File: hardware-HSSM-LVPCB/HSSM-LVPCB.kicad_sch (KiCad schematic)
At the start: 56 parts, among them J1 UFL_R_SMT_1_10, J2 LPPB061NGCN-RC, Q1 Q_MOSFET_N_BSS123, Q2 Q_MOSFET_N_BSS123, U1 ESP32-C6, U2 W25Q64JVSSIQ_SOIC-8, X1 X_40MHz_SMD_ECS-2520SMV-400-F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

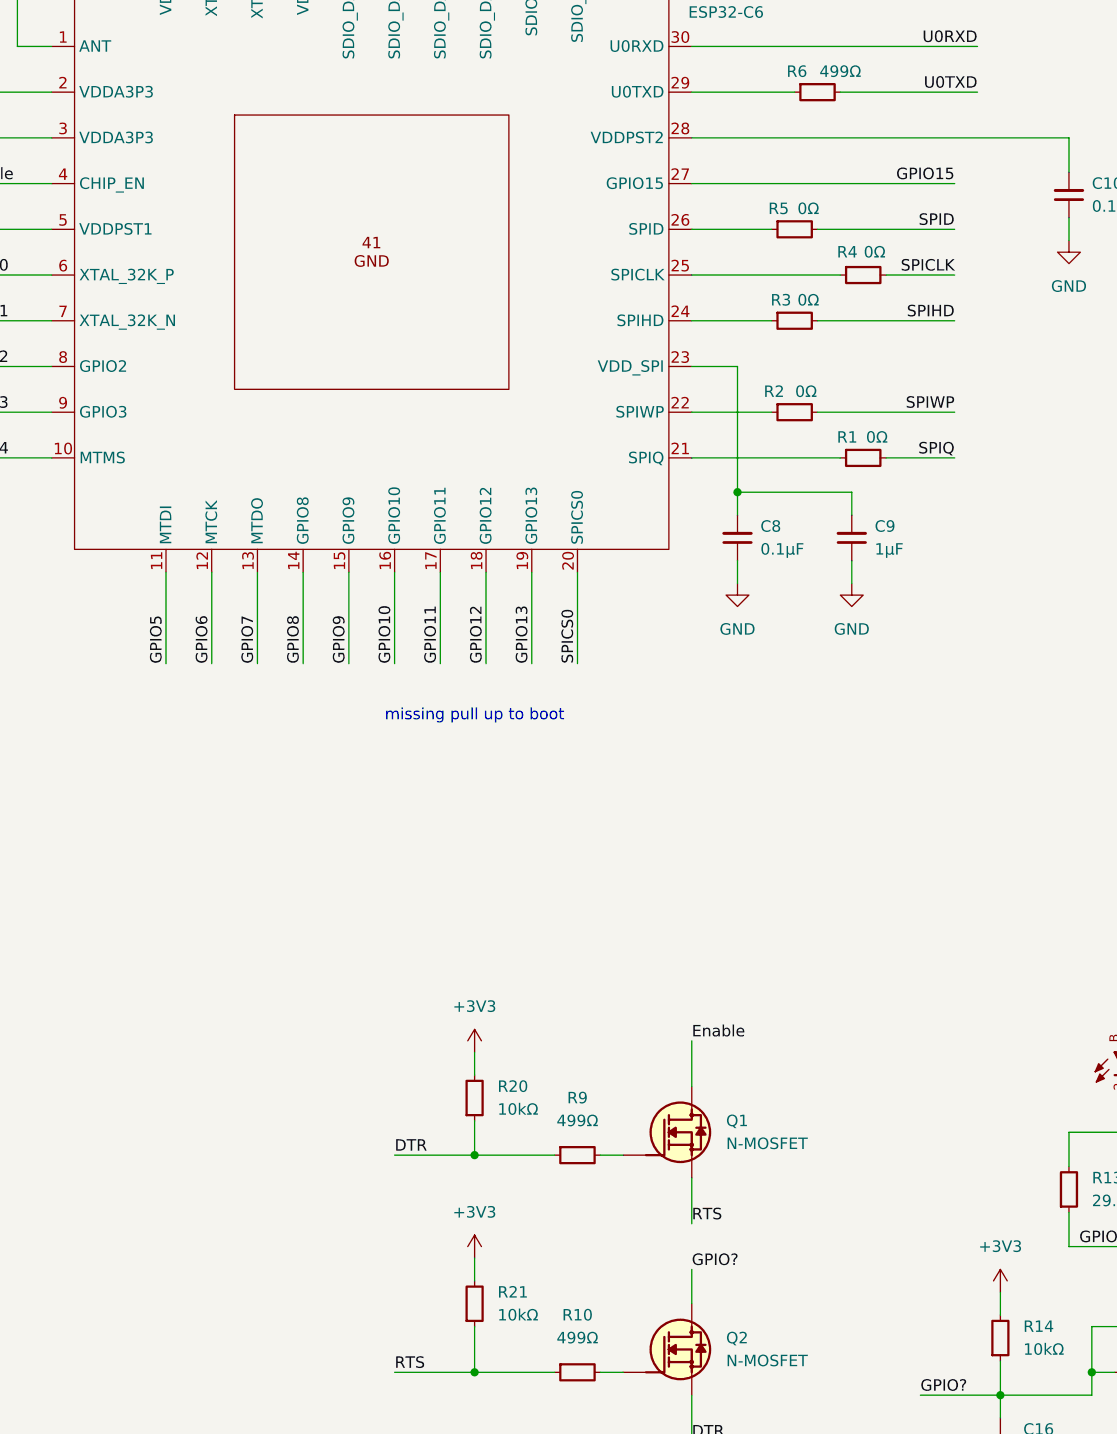
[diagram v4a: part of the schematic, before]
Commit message: [#4] SCH ESP32-C6 set pins for boot
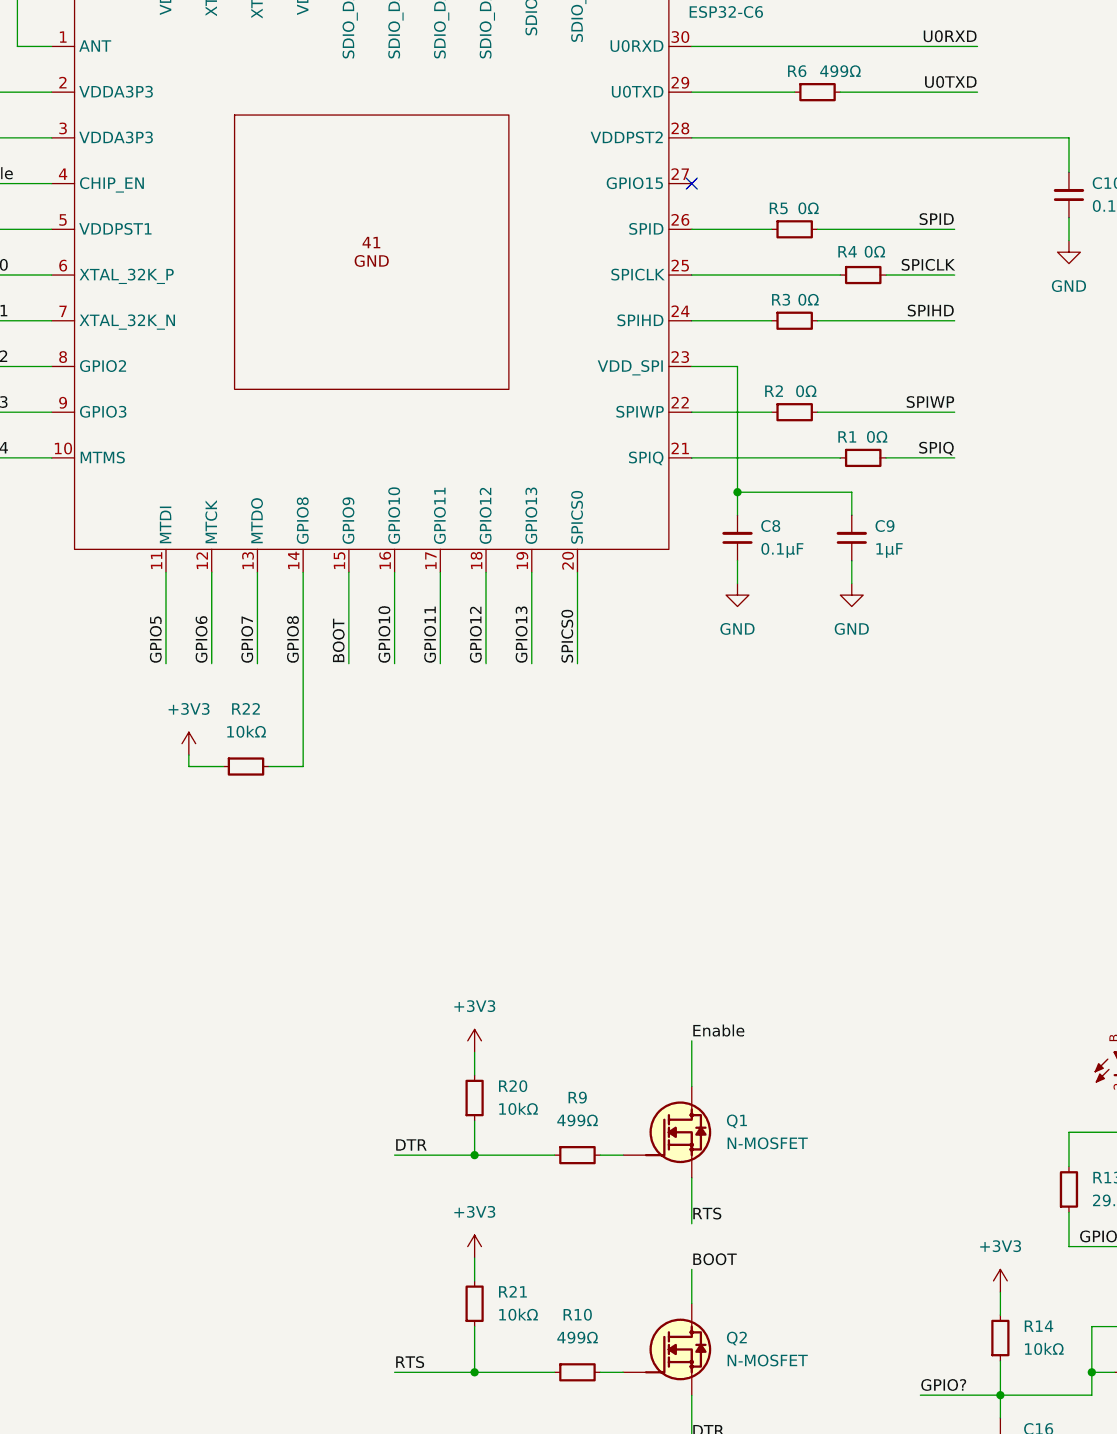
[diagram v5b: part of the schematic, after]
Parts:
- added R22: R_10k_1pct_0402_RC0402FR-0710KL, HSSM-LVPCB:R_0402, symbol HSSM-LVPCB:R_10k_1pct_0402_RC0402FR-0710KL
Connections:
- net +3V3: now also R22.1
- net GPIO8: now also R22.2
- net GPIO?: no longer Q2.3 (D)
- net GPIO15: no longer names the net of U1.27 (GPIO15)
- net GPIO9 renamed BOOT
- net BOOT: now also Q2.3 (D)
- no-connect marks 0 -> 1
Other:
- note removed: "missing pull up to boot"
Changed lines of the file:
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@@
 		(color 0 0 0 0)
 	)
+	(no_connect
+		(at 175.26 111.76)
+	)
 	(wire
 		(pts
@@
 	(wire
 		(pts
-			(xy 137.16 165.1) (xy 137.16 154.94)
-		)
-		(stroke
-			(width 0)
-			(type default)
-		)
-	)
-	(wire
-		(pts
 			(xy 29.21 106.68) (xy 29.21 110.49)
 		)
@@
 	(wire
 		(pts
-			(xy 132.08 165.1) (xy 132.08 154.94)
-		)
-		(stroke
-			(width 0)
-			(type default)
-		)
-	)
-	(wire
-		(pts
 			(xy 351.79 212.09) (xy 336.55 212.09)
 		)
@@
 	(wire
 		(pts
+			(xy 123.19 176.53) (xy 119.38 176.53)
+		)
+		(stroke
+			(width 0)
+			(type default)
+		)
+	)
+	(wire
+		(pts
 			(xy 77.47 52.07) (xy 77.47 49.53)
 		)
@@
 	(wire
 		(pts
+			(xy 128.27 176.53) (xy 132.08 176.53)
+		)
+		(stroke
+			(width 0)
+			(type default)
+		)
+	)
+	(wire
+		(pts
 			(xy 190.5 41.91) (xy 193.04 41.91)
 		)
@@
 	(wire
 		(pts
+			(xy 137.16 154.94) (xy 137.16 165.1)
+		)
+		(stroke
+			(width 0)
+			(type default)
+		)
+	)
+	(wire
+		(pts
 			(xy 377.19 217.17) (xy 379.73 217.17)
 		)
@@
 	(wire
 		(pts
+			(xy 119.38 176.53) (xy 119.38 175.26)
+		)
+		(stroke
+			(width 0)
+			(type default)
+		)
+	)
+	(wire
+		(pts
 			(xy 223.52 217.17) (xy 217.17 217.17)
 		)
@@
 	(wire
 		(pts
+			(xy 132.08 154.94) (xy 132.08 176.53)
+		)
+		(stroke
+			(width 0)
+			(type default)
+		)
+	)
+	(wire
+		(pts
 			(xy 29.21 115.57) (xy 29.21 119.38)
 		)
@@
 	(wire
 		(pts
-			(xy 175.26 111.76) (xy 204.47 111.76)
-		)
-		(stroke
-			(width 0)
-			(type default)
-		)
-	)
-	(wire
-		(pts
 			(xy 231.14 45.72) (xy 218.44 45.72)
 		)
@@
 		)
 	)
-	(text "missing pull up to boot\n"
-		(exclude_from_sim no)
-		(at 151.13 170.942 0)
-		(effects
-			(font
-				(size 1.27 1.27)
-			)
-		)
-	)
 	(text "S1 button"
 		(exclude_from_sim no)
@@
 		)
 	)
-	(label "GPIO9"
+	(label "BOOT"
 		(at 137.16 165.1 90)
 		(fields_autoplaced yes)
@@
 		)
 	)
+	(label "BOOT"
+		(at 175.26 232.41 0)
+		(fields_autoplaced yes)
+		(effects
+			(font
+				(size 1.27 1.27)
+			)
+			(justify left bottom)
+		)
+	)
 	(label "GPIO4"
 		(at 93.98 142.24 0)
@@
 		)
 	)
+	(label "GPIO8"
+		(at 132.08 165.1 90)
+		(fields_autoplaced yes)
+		(effects
+			(font
+				(size 1.27 1.27)
+			)
+			(justify left bottom)
+		)
+	)
 	(label "GPIO_S1"
 		(at 232.41 144.78 0)
@@
 		)
 	)
-	(label "GPIO?"
-		(at 175.26 232.41 0)
-		(fields_autoplaced yes)
-		(effects
-			(font
-				(size 1.27 1.27)
-			)
-			(justify left bottom)
-		)
-	)
-	(label "GPIO8"
-		(at 132.08 165.1 90)
-		(fields_autoplaced yes)
-		(effects
-			(font
-				(size 1.27 1.27)
-			)
-			(justify left bottom)
-		)
-	)
 	(label "GPIO7"
 		(at 127 165.1 90)
@@
 		)
 	)
-	(label "GPIO15"
-		(at 204.47 111.76 180)
-		(fields_autoplaced yes)
-		(effects
-			(font
-				(size 1.27 1.27)
-			)
-			(justify right bottom)
-		)
-	)
 	(label "DEV_RX"
 		(at 240.03 154.94 0)
@@
 	)
 	(symbol
+		(lib_id "power:+3V3")
+		(at 119.38 175.26 0)
+		(unit 1)
+		(exclude_from_sim no)
+		(in_bom yes)
+		(on_board yes)
+		(dnp no)
+		(fields_autoplaced yes)
+		(property "Reference" "#PWR027"
+			(at 119.38 179.07 0)
+			(effects
+				(font
+					(size 1.27 1.27)
+				)
+				(hide yes)
+			)
+		)
+		(property "Value" "+3V3"
+			(at 119.38 170.18 0)
+			(effects
+				(font
+					(size 1.27 1.27)
+				)
+			)
+		)
+		(property "Footprint" ""
+			(at 119.38 175.26 0)
+			(effects
+				(font
+					(size 1.27 1.27)
+				)
+				(hide yes)
+			)
+		)
+		(property "Datasheet" ""
+			(at 119.38 175.26 0)
+			(effects
+				(font
+					(size 1.27 1.27)
+				)
+				(hide yes)
+			)
+		)
+		(property "Description" "Power symbol creates a global label with name \"+3V3\""
+			(at 119.38 175.26 0)
+			(effects
+				(font
+					(size 1.27 1.27)
+				)
+				(hide yes)
+			)
+		)
+		(pin "1"
+		)
+		(instances
+			(project ""
+				(path "/77e28373-c8b2-479f-b36e-df59d529ffba"
+					(reference "#PWR027")
+					(unit 1)
+				)
+			)
+		)
+	)
+	(symbol
 		(lib_id "power:GND")
 		(at 193.04 156.21 0)
@@
 					(unit 1)
 				)
+			)
+		)
+	)
+	(symbol
+		(lib_id "HSSM-LVPCB:R_10k_1pct_0402_RC0402FR-0710KL")
+		(at 125.73 176.53 0)
+		(unit 1)
+		(exclude_from_sim no)
+		(in_bom yes)
+		(on_board yes)
+		(dnp no)
+		(fields_autoplaced yes)
+		(property "Reference" "R22"
+			(at 125.73 170.18 0)
+			(effects
+				(font
+					(size 1.27 1.27)
+					(thickness 0.15)
+				)
+			)
+		)
+		(property "Value" "R_10k_1pct_0402_RC0402FR-0710KL"
+			(at 125.73 184.404 0)
+			(effects
+				(font
+					(size 1.27 1.27)
+					(thickness 0.15)
+				)
+				(justify left bottom)
+				(hide yes)
+			)
+		)
+		(property "Footprint" "HSSM-LVPCB:R_0402"
+			(at 125.73 186.944 0)
+			(effects
+				(font
+					(size 1.27 1.27)
+					(thickness 0.15)
+				)
+				(justify left bottom)
+				(hide yes)
+			)
+		)
+		(property "Datasheet" "https://www.yageo.com/upload/media/product/products/datasheet/rchip/PYu-RC_Group_51_RoHS_L_12.pdf"
+			(at 125.73 189.484 0)
+			(effects
+				(font
+					(size 1.27 1.27)
+					(thickness 0.15)
+				)
+				(justify left bottom)
+				(hide yes)
+			)
+		)
+		(property "Description" "SMD Thick Film Resistor, 10kΩ, ±1%, 0.063W, 0402"
+			(at 125.73 176.53 0)
+			(effects
+				(font
+					(size 1.27 1.27)
+				)
+				(hide yes)
+			)
+		)
+		(property "MPN" "RC0402FR-0710KL"
+			(at 125.73 192.024 0)
+			(effects
+				(font
+					(size 1.27 1.27)
+					(thickness 0.15)
+				)
+				(justify left bottom)
+				(hide yes)
+			)
+		)
+		(property "Manufacturer" "Yageo"
+			(at 125.73 194.564 0)
+			(effects
+				(font
+					(size 1.27 1.27)
+					(thickness 0.15)
+				)
+				(justify left bottom)
+				(hide yes)
+			)
+		)
+		(property "License" "Apache-2.0"
+			(at 125.73 197.104 0)
+			(effects
+				(font
+					(size 1.27 1.27)
+				)
+				(justify left bottom)
+				(hide yes)
+			)
+		)
+		(property "Author" "Lukasz Nowarkiewicz"
+			(at 125.73 199.644 0)
+			(effects
+				(font
+					(size 1.27 1.27)
+				)
+				(justify left bottom)
+				(hide yes)
+			)
+		)
+		(property "Val" "10kΩ"
+			(at 125.73 172.72 0)
+			(effects
+				(font
+					(size 1.27 1.27)
+				)
+			)
+		)
+		(pin "2"
+		)
+		(pin "1"
+		)
+		(instances
+			(project "HSSM-LVPCB"
+				(path "/77e28373-c8b2-479f-b36e-df59d529ffba"
+					(reference "R22")
+					(unit 1)
+				)
